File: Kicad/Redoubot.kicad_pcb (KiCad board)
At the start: 4 copper layers, 98 parts, among them J1 HM_10_BLE_Module, J10 VL53L0CXV0DH - TOF, J11 DFPlayer_Left, J12 Speaker, J13 DFPlayer_Right, J14 USB_C_Receptacle_USB2.0_16P, J15 Conn_ST_STDC14, J2 Connecteur batterie, J3 APDS9960, J4 Neopixel, J5 Motor_Left, J6 Motor_Right, J7 MPU-6050, J8 Servo_Left, J9 Servo_Right, Q1 DMP1045UQ-7, U1 STM32G431RBTx, U2 LD39050PU33R, U3 BQ25896RTWR, U4 BQ27220YZFR, U5 DRV8833PWP, U7 DMN313DLT-7, U8 MMDT2907A-7-F, Y1 8MHz

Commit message: feat: added the ground plane
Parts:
- moved C23 54.1 mm to (118.5, 116.2)
- moved JP5 1.75 mm to (126.7, 77.7)
- moved R1 1.32 mm to (132.5, 86.2)
- moved C10 0.77 mm to (138.8, 81.2), turned to 180 degrees
- moved R6 0.66 mm to (135.0, 84.5), turned to 90 degrees
- moved C12 0.35 mm to (138.9, 79.6)
- moved C5 0.26 mm to (131.8, 79.4), turned to 90 degrees
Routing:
- net +5V: track 23.7 -> 54.3 mm
- net +3.3V: track 20.7 -> 42.6 mm
- net GND: track 0.11 -> 10.6 mm, vias 0 -> 3
- net Net-(JP5-A): track 5.08 -> 6.43 mm
- net VCC: track 19.4 -> 18.3 mm
- net /Power_management/BAT_CHG: track 18.3 -> 17.6 mm
- added copper zone on In2.Cu, net +3.3V
- added copper zone on In2.Cu, net +5V
- added copper zone on B.Cu, net GND
- added copper zone on F.Cu, net GND
- added copper zone on In1.Cu, net GND
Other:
- board outline added: 90 x 90 mm

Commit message: feat: continued with the routing
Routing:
- net /SCL_BAT: track 4.46 -> 42.0 mm
- net /SDA_BAT: track 5.39 -> 42.2 mm
- net GND: track 10.6 -> 22.4 mm, vias 3 -> 12
- net Net-(U3-TS): track 3.28 -> 13.7 mm, vias 1 -> 2

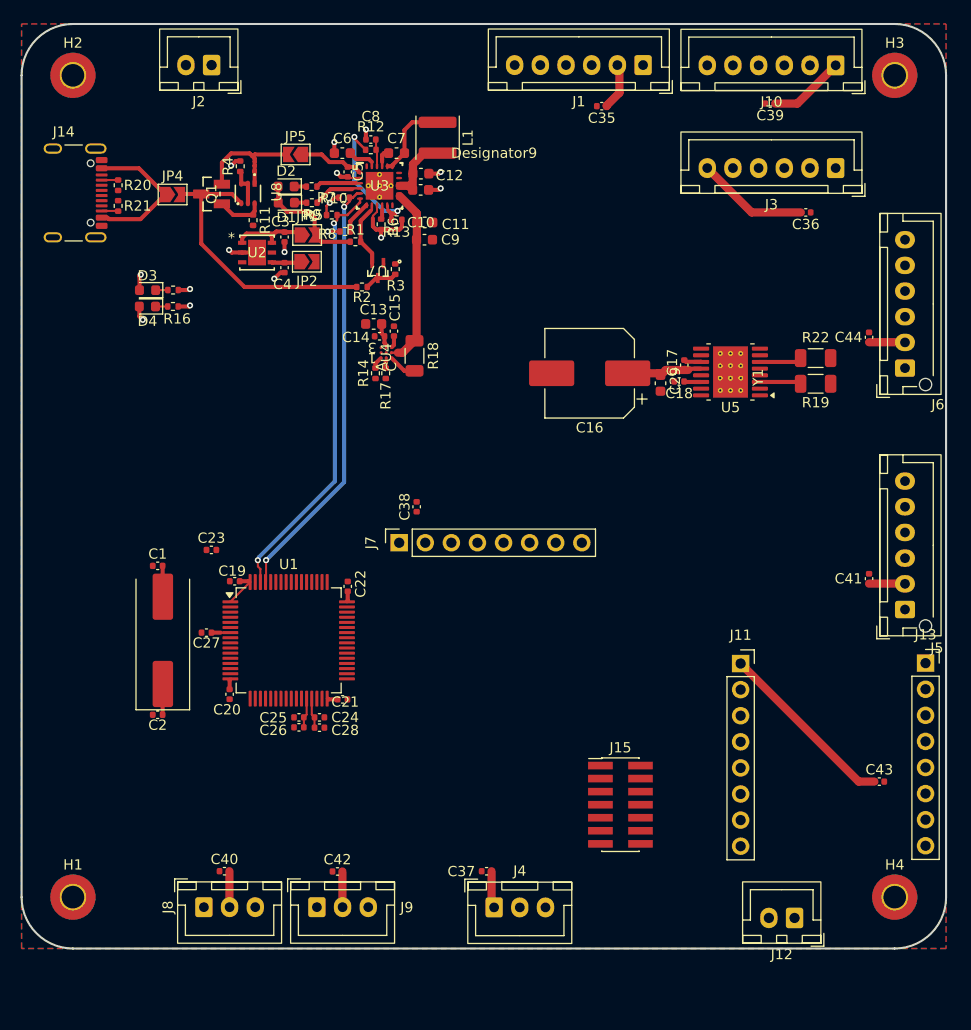
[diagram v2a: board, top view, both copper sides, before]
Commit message: feat: added routing for most of the connectors
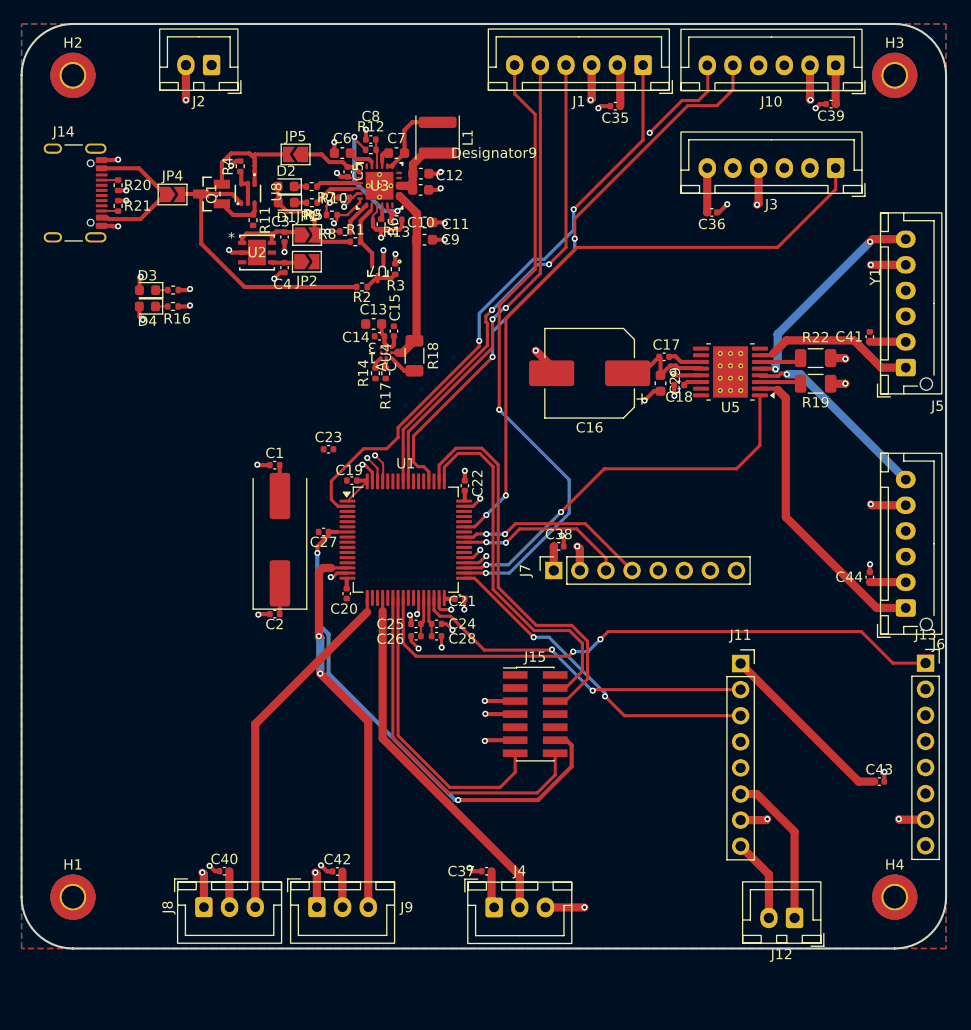
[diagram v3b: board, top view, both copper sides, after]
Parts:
- moved C41 23.6 mm to (182.6, 95.5)
- moved J5 23.6 mm to (186.1, 98.5)
- moved C44 23.4 mm to (182.6, 118.8)
- moved J6 23.4 mm to (186.1, 121.8)
- moved J7 15.3 mm to (151.8, 118.2)
- moved C1 15.0 mm to (124.7, 108.0)
- moved C19 15.0 mm to (132.2, 109.5)
- moved C2 15.0 mm to (124.7, 122.5)
- moved C20 15.0 mm to (131.7, 120.5)
- moved C21 15.0 mm to (142.7, 121.0)
- moved C22 15.0 mm to (143.2, 110.0)
- moved C27 15.0 mm to (129.4, 114.5)
- moved U1 15.0 mm to (137.4, 115.2)
- moved Y1 15.0 mm to (125.2, 115.2)
- moved C23 15.0 mm to (129.9, 106.4)
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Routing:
- net GND: track 22.4 -> 120.8 mm, vias 12 -> 63
- net /INT_ADA: track 0.00 -> 61.9 mm, vias 0 -> 2
- net /BRK_HM10: track 0.00 -> 61.4 mm, vias 0 -> 2
- net /STATE_HM10: track 0.00 -> 58.7 mm, vias 0 -> 2
- net /GPIO_BUSY: track 0.00 -> 58.1 mm, vias 0 -> 2
- net /GPIO_TOF: track 0.00 -> 56.0 mm, vias 0 -> 2
- net /STM32/NRST: track 1.84 -> 50.5 mm, vias 0 -> 2
- net /TXD_HM10: track 0.00 -> 47.9 mm, vias 0 -> 2
- net /RXD_HM10: track 0.00 -> 46.0 mm, vias 0 -> 2
- net /STM32/STLINK_SWCLK: track 0.00 -> 39.2 mm
- net /GPIO_NSLEEP: track 0.00 -> 38.6 mm, vias 0 -> 2
- net /PWM_SERVO_R: track 0.00 -> 37.6 mm, vias 0 -> 2
- net /SCL_BAT: track 42.0 -> 5.19 mm
- net /STM32/STLINK_SWDIO: track 0.00 -> 36.1 mm
- net /PWM_NEOPIXEL: track 0.00 -> 35.7 mm
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
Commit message: chore: modified some routes to reduce the space taken on the other side of the board
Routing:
- net /Motor_Driver/MR-: track 18.6 -> 19.5 mm, vias 1 -> 2
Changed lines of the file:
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@@
+	)
+	(segment
+		(start 175.65 101.8)
+		(end 183.2 109.35)
+		(width 0.8)
+		(layer "F.Cu")
+		(net "/Motor_Driver/MR-")
 	)
 	(segment
@@
 		(end 171.95 99.275)
 		(width 0.35)
+		(layer "F.Cu")
+		(net "/Motor_Driver/MR-")
+	)
+	(segment
+		(start 183.2 109.35)
+		(end 186.075 109.35)
+		(width 0.8)
 		(layer "F.Cu")
 		(net "/Motor_Driver/MR-")
@@
 		(net "/Motor_Driver/MR-")
 	)
+	(via
+		(at 175.65 101.8)
+		(size 0.6)
+		(drill 0.3)
+		(layers "F.Cu" "B.Cu")
+		(net "/Motor_Driver/MR-")
+	)
 	(segment
-		(start 174.5 99.1)
-		(end 175.825 99.1)
+		(start 175.65 100.25)
+		(end 175.65 101.8)
 		(width 0.8)
 		(layer "B.Cu")
@@
 	)
 	(segment
-		(start 175.825 99.1)
-		(end 186.075 109.35)
+		(start 174.5 99.1)
+		(end 175.65 100.25)
 		(width 0.8)
 		(layer "B.Cu")
@@
 	)
 	(segment
-		(start 182.85 85.95)
-		(end 182.6 86.2)
-		(width 0.8)
-		(layer "F.Cu")
-		(net "/Motor_Driver/ML-")
-	)
-	(segment
-		(start 186.075 85.95)
+		(start 173.45 95.35)
 		(end 182.85 85.95)
 		(width 0.8)
@@
 	)
 	(segment
+		(start 182.85 85.95)
+		(end 186.075 85.95)
+		(width 0.8)
+		(layer "F.Cu")
+		(net "/Motor_Driver/ML-")
+	)
+	(segment
+		(start 173.4 95.35)
+		(end 173.45 95.35)
+		(width 0.8)
+		(layer "F.Cu")
+		(net "/Motor_Driver/ML-")
+	)
+	(segment
 		(start 173.35 98.55)
 		(end 171.875 98.55)
@@
 	)
 	(via
-		(at 182.6 86.2)
+		(at 173.4 95.35)
 		(size 0.6)
 		(drill 0.3)
@@
 	)
 	(segment
-		(start 173.6 95.2)
-		(end 182.6 86.2)
+		(start 173.4 98.6)
+		(end 173.4 95.35)
 		(width 0.8)
 		(layer "B.Cu")
-		(net "/Motor_Driver/ML-")
-	)
-	(segment
-		(start 173.4 98)
-		(end 173.6 97.8)
-		(width 0.8)
-		(layer "B.Cu")
-		(net "/Motor_Driver/ML-")
-	)
-	(segment
-		(start 173.6 97.8)
-		(end 173.6 95.2)
-		(width 0.8)
-		(layer "B.Cu")
-		(net "/Motor_Driver/ML-")
-	)
-	(segment
-		(start 173.4 98.6)
-		(end 173.4 98)
-		(width 0.8)
-		(layer "B.Cu")

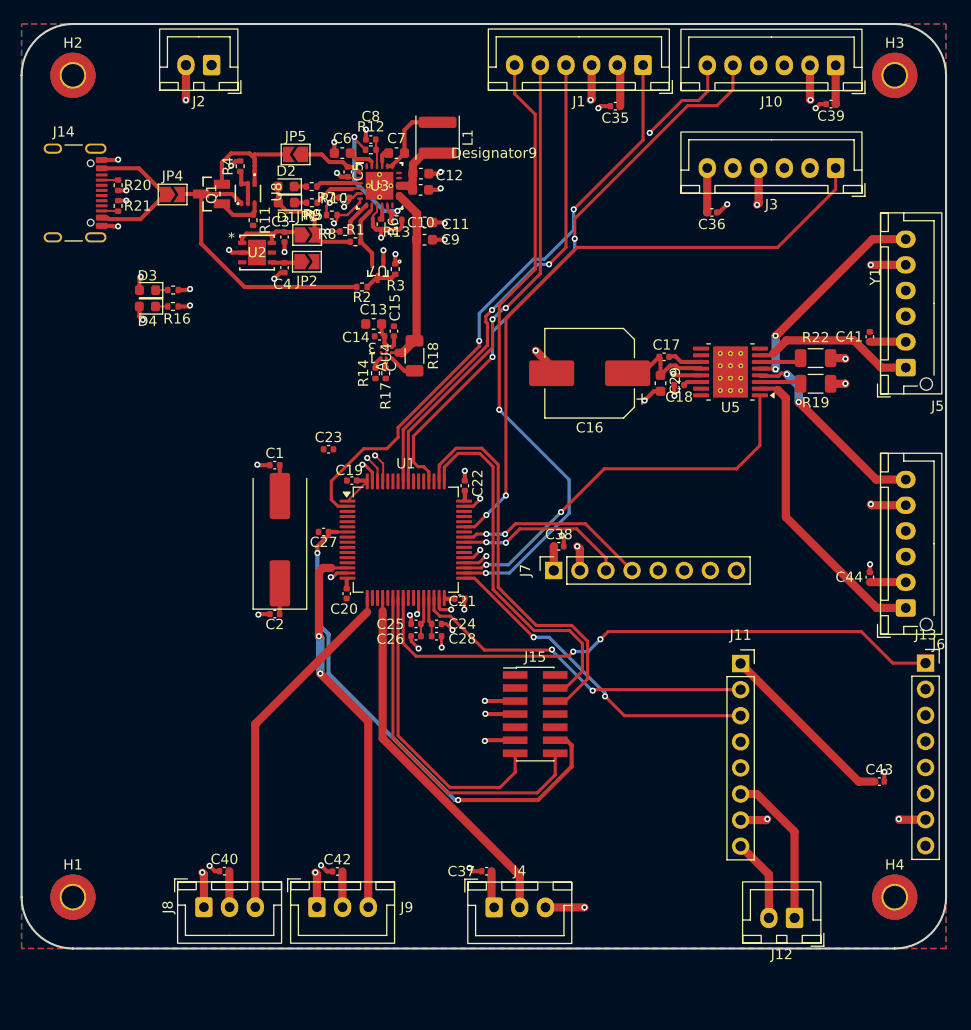
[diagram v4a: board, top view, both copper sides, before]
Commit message: Feet: finished wiring pcb
53 errors are normal and can be ignored, but should be fixed. PCB can be shrunk by a decent amount.
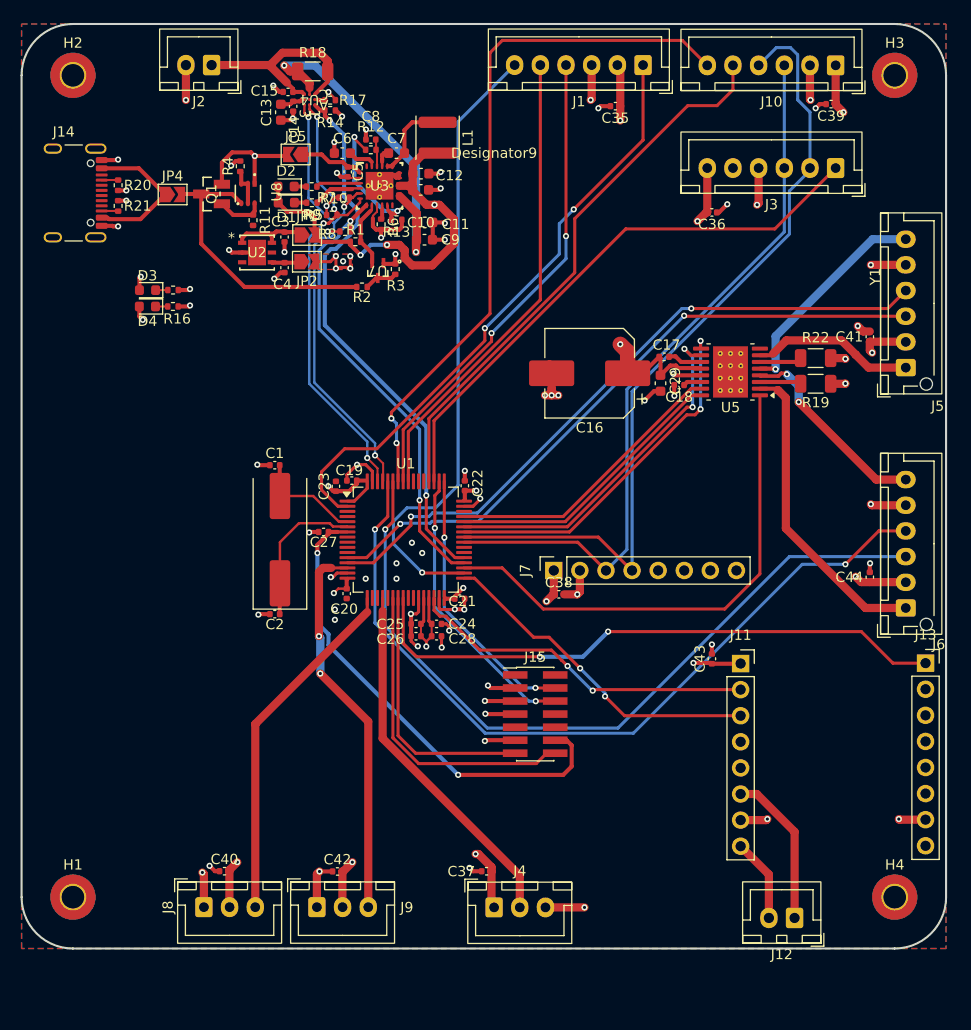
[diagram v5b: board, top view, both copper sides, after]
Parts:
- moved R18 29.4 mm to (128.3, 69.6), turned to 0 degrees
- moved R17 27.1 mm to (130.0, 72.4), turned to 180 degrees
- moved R14 26.0 mm to (130.0, 73.4), turned to 180 degrees
- moved U4 25.7 mm to (128.0, 72.4), turned to 180 degrees
- moved C15 25.5 mm to (125.9, 71.6), turned to 180 degrees
- moved C14 23.9 mm to (126.4, 73.0), turned to -90 degrees
- moved C13 22.5 mm to (125.2, 73.6), turned to -90 degrees
- moved C43 20.2 mm to (167.2, 126.8), turned to 90 degrees
- moved C38 4.68 mm to (152.3, 120.5)
- moved C23 3.67 mm to (130.6, 110.0), turned to 90 degrees
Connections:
- U1 pad 10: /PWM1_MR -> unconnected-(U1-PC2-Pad10)
- U1 pad 11: /PWM2_MR -> unconnected-(U1-PC3-Pad11)
- U1 pad 42: unconnected-(U1-PA8-Pad42) -> /PWM1_ML
- U1 pad 43: /INT_ADA -> /PWM2_ML
- U1 pad 44: unconnected-(U1-PA10-Pad44) -> /PWM1_MR
- U1 pad 45: unconnected-(U1-PA11-Pad45) -> /PWM2_MR
- U1 pad 51: unconnected-(U1-PA15-Pad51) -> /INT_ADA
- U1 pad 8: /PWM1_ML -> unconnected-(U1-PC0-Pad8)
- U1 pad 9: /PWM2_ML -> unconnected-(U1-PC1-Pad9)
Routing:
- net +5V: track 58.4 -> 274.6 mm, vias 1 -> 9
- net /Enc_B_R: track 0.00 -> 78.6 mm, vias 0 -> 2
- net /Enc_A_R: track 0.00 -> 76.1 mm, vias 0 -> 1
- net /Enc_B_L: track 0.00 -> 65.8 mm, vias 0 -> 2
- net /Enc_A_L: track 0.00 -> 64.1 mm, vias 0 -> 2
- net /SDA_ADA: track 18.8 -> 80.4 mm, vias 2 -> 0
- net /XSHUT_TOF: track 9.87 -> 68.6 mm, vias 1 -> 2
- net /SCL_ADA: track 16.8 -> 71.3 mm, vias 2 -> 0
- net /GPOUT_FG: track 3.06 -> 53.7 mm, vias 1 -> 2
- net /SCL_BAT: track 5.19 -> 46.3 mm, vias 2 -> 3
- net /GPIO_PWR_INT: track 5.66 -> 44.6 mm, vias 1 -> 2
- net /SDA_BAT: track 6.87 -> 45.2 mm, vias 2 -> 4
- net /PWM1_ML: track 0.00 -> 35.4 mm, vias 0 -> 2
- net /PWM2_ML: track 0.00 -> 35.0 mm, vias 0 -> 2
- net /PWM2_MR: track 0.00 -> 28.2 mm
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- added copper zone on F.Cu, net +3.3V
- removed copper zone on In2.Cu, net +5V

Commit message: Chore: Changements M. Fiack
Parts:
- H1, H2, H3, H4: footprint MountingHole:MountingHole_2.2mm_M2_Pad_TopBottom -> MountingHole:MountingHole_3.2mm_M3_ISO7380_Pad_TopBottom
- J5, J6: footprint Connector_JST:JST_XH_B6B-XH-AM_1x06_P2.50mm_Vertical -> Connector_JST:JST_XH_B6B-XH-A_1x06_P2.50mm_Vertical
- moved R14 0.07 mm to (130.1, 73.4), turned to 0 degrees
- moved R17 0.05 mm to (130.1, 72.4)
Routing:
- net GND: track 141.1 -> 142.6 mm
- net /GPOUT_FG: track 53.7 -> 54.6 mm, vias 2 -> 3
- net +3.3V: track 59.8 -> 58.9 mm, vias 19 -> 18
- net /Power_management/BAT: track 20.9 -> 21.6 mm

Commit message: Feat : Finished wiring pcb
shrunk pcb and fixed issues
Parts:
- U4: footprint footprints_BQ27:YZF9_TEX -> Package_BGA:BGA-9_1.6x1.6mm_Layout3x3_P0.5mm
- moved J8 58.9 mm to (108.3, 92.8), turned to -90 degrees
- moved C40 53.2 mm to (111.8, 94.9), turned to -90 degrees
- moved J9 51.4 mm to (108.3, 103.8), turned to -90 degrees
- moved J4 48.2 mm to (108.2, 121.1), turned to -90 degrees
- moved C42 45.8 mm to (111.8, 105.8), turned to -90 degrees
- moved C37 43.1 mm to (111.8, 120.4), turned to 90 degrees
- moved J12 37.0 mm to (144.6, 131.3), turned to 0 degrees
- moved D3 36.8 mm to (141.2, 68.1), turned to 90 degrees
- moved D4 36.7 mm to (139.6, 68.1), turned to 90 degrees
- moved R15 33.3 mm to (141.2, 70.6), turned to -90 degrees
- moved R16 33.1 mm to (139.6, 70.6), turned to -90 degrees
- moved C43 20.9 mm to (149.7, 115.3)
- moved J11 20.9 mm to (152.5, 115.7)
- moved J13 20.9 mm to (170.5, 115.7)
- moved H1 17.5 mm to (105.0, 132.5)
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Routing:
- net +5V: track 274.6 -> 202.0 mm
- net /GPIO_BUSY: track 58.1 -> 40.1 mm, vias 2 -> 1
- net /RX_DF: track 34.3 -> 16.9 mm, vias 2 -> 1
- net /GPIO_NSLEEP: track 49.3 -> 31.9 mm
- net GND: track 142.6 -> 128.2 mm, vias 73 -> 68
- net /PWM_SERVO_R: track 37.6 -> 24.5 mm, vias 2 -> 1
- net /TX_DF: track 32.6 -> 19.8 mm, vias 2 -> 0
- net /BRK_HM10: track 61.2 -> 49.4 mm
- net /SDA_BAT: track 45.2 -> 35.4 mm
- net /SCL_BAT: track 46.3 -> 36.5 mm
- net /RXD_HM10: track 45.8 -> 36.2 mm
- net /XSHUT_TOF: track 68.6 -> 59.7 mm
- net /GPIO_TOF: track 54.4 -> 45.6 mm
- net /GPOUT_FG: track 54.6 -> 46.4 mm, vias 3 -> 2
- net /GPIO_PWR_INT: track 44.6 -> 36.8 mm
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- added copper zone on In2.Cu, net +5V
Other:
- board size 90 x 90 mm -> 90 x 72.5 mm

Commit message: Feat: added silkscreen and logo
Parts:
- added G***: LOGO, Logo:Logo silk 30, F.Cu at (126.3, 125.6)
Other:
- board text added: "B"
- board text added: "E-MENPIOT G-LOISELET G-VIDON J-MANSARD L-FIACK {dblquote}---->"
- board text added: "F"
- board text added: "G"
- board text added: "P"
